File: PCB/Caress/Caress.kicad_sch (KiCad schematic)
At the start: 23 parts, among them J1 Conn_01x04_Male_Cell, J10 Conn_01x01_Male, J11 Conn_01x01_Male, J12 Conn_01x01_Male, J13 Conn_01x01_Male, J2 Conn_01x01_Male, J3 Conn_01x01_Male, J4 Conn_01x03_Male_AX12A, J5 Conn_01x02_Male_12V, J6 Conn_01x01_Male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

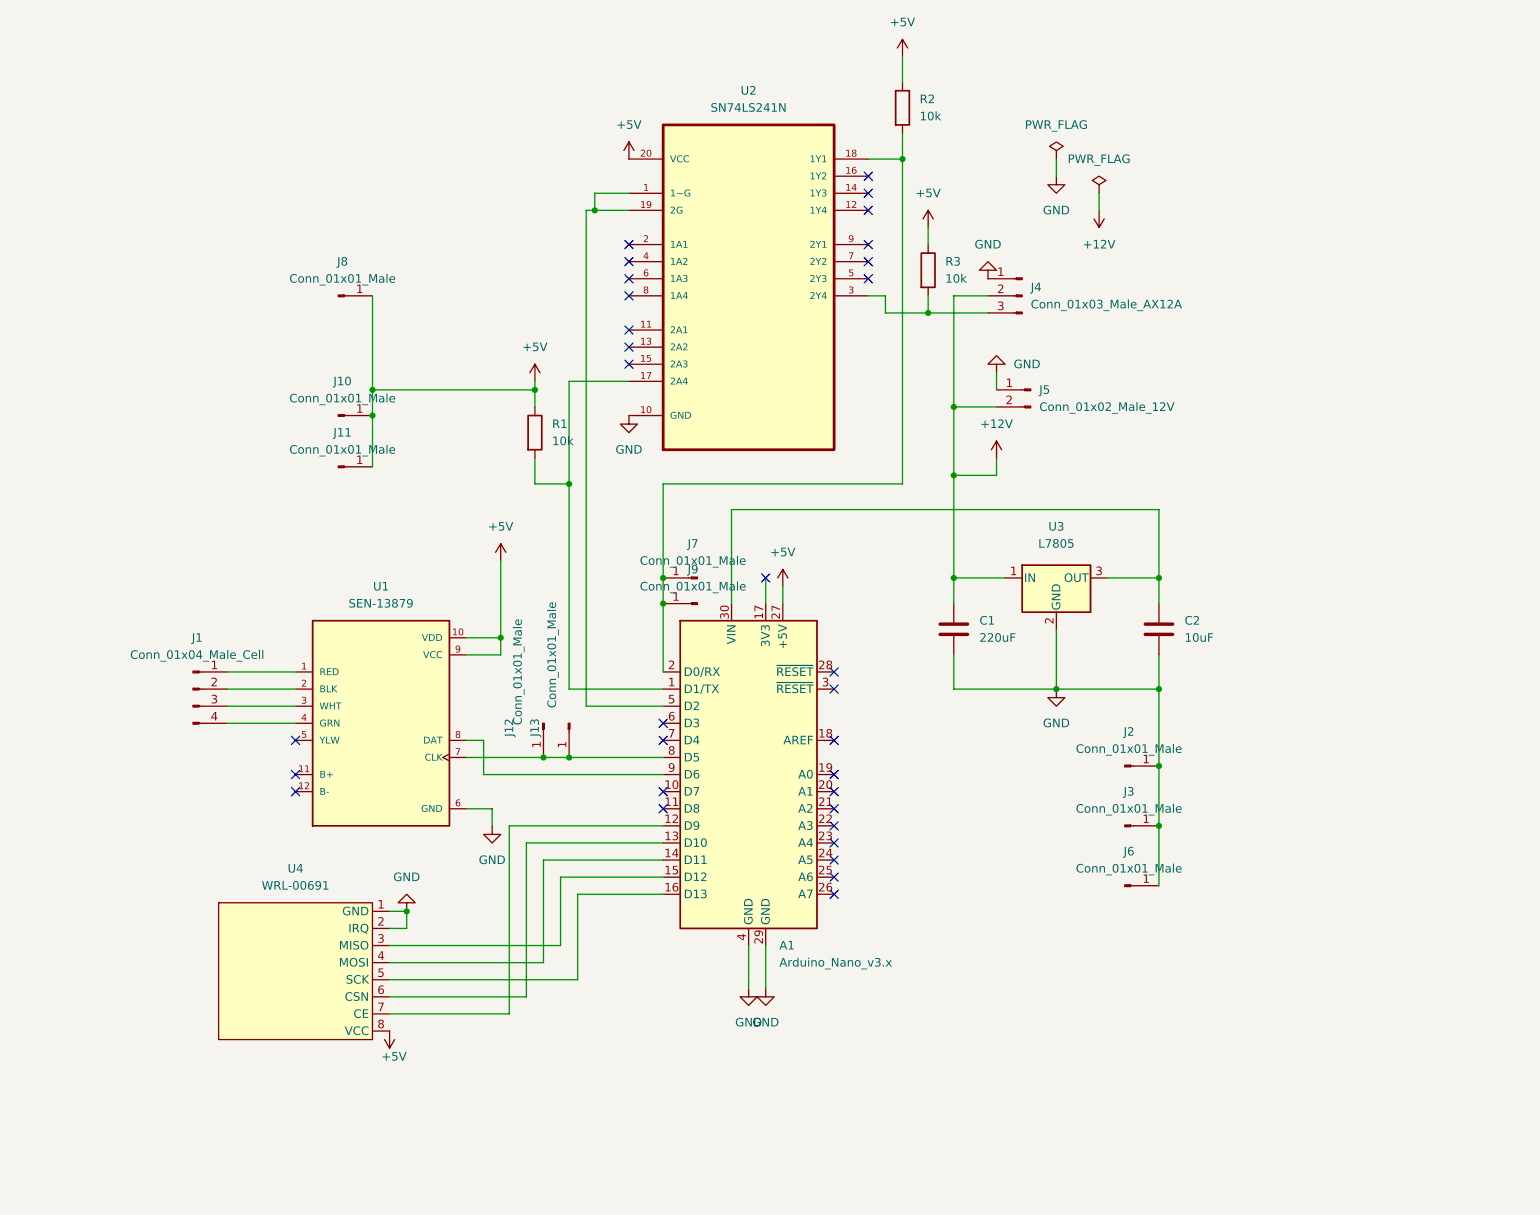
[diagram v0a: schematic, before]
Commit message: Updated PCB files; added desing files for caress and vibration
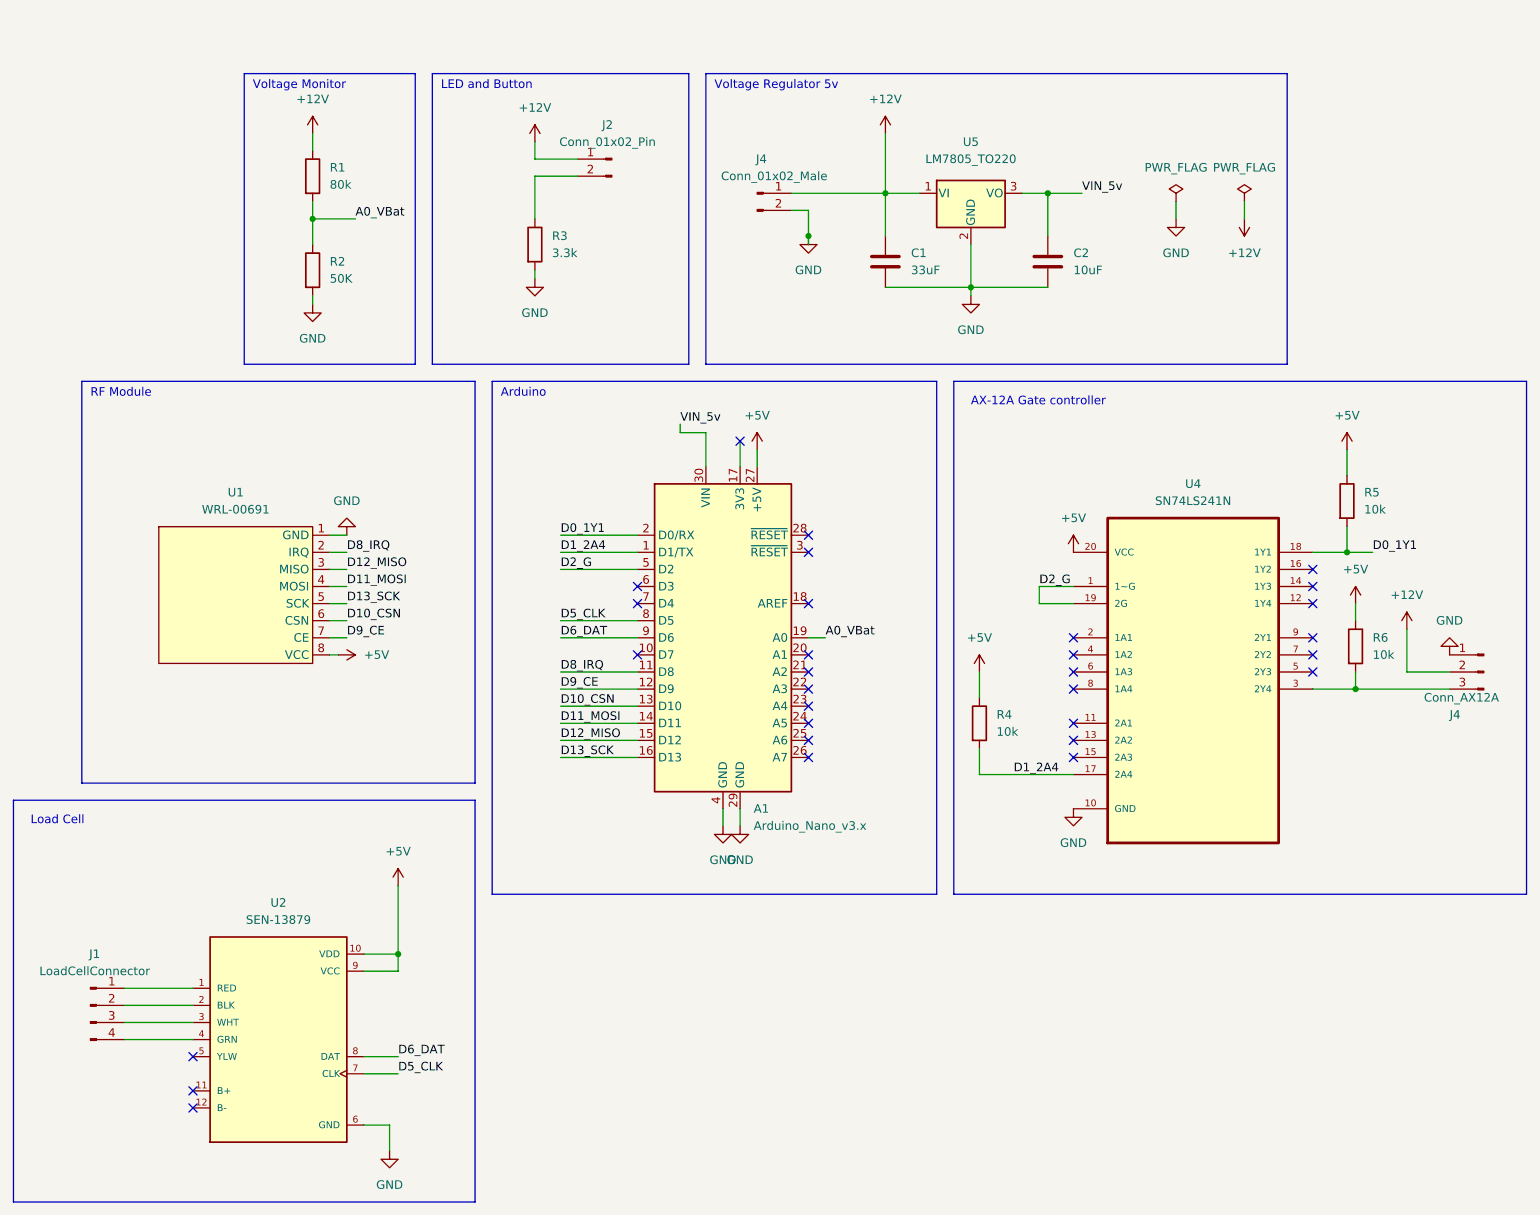
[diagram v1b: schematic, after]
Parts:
- removed J10, J11, J12, J13, J2, J3, J6, J7, J8, J9: Conn_01x01_Male, Connector_PinHeader_2.00mm:PinHeader_1x01_P2.00mm_Vertical, symbol Connector:Conn_01x01_Male
- removed J5: Conn_01x02_Male_12V, Connector_PinSocket_2.54mm:PinSocket_1x02_P2.54mm_Vertical, symbol Connector:Conn_01x02_Male
- removed U1: SEN-13879, SEN-13879:SPARKFUN_SEN-13879, symbol SEN-13879:SEN-13879
- removed U2: SN74LS241N, Package_DIP:DIP-20_W7.62mm_Socket, symbol SN74LS241N:SN74LS241N
- removed U3: L7805, Package_TO_SOT_THT:TO-220-3_Vertical, symbol Regulator_Linear:L7805
- removed U4: WRL-00691, SEN-13879:WRL-00691, symbol SN74LS241N:WRL-00691
- added J2: Conn_01x02_Pin, Connector_JST:JST_EH_B2B-EH-A_1x02_P2.50mm_Vertical, symbol Connector:Conn_01x02_Pin
- added J4: Conn_01x02_Male, Connector_JST:JST_EH_B2B-EH-A_1x02_P2.50mm_Vertical, symbol Connector:Conn_01x02_Male
- added R4, R5, R6: 10k, Resistor_THT:R_Axial_DIN0207_L6.3mm_D2.5mm_P7.62mm_Horizontal, symbol Device:R
- added U1: WRL-00691, Mods:WRL-00691, symbol SN74LS241N:WRL-00691
- added U2: SEN-13879, Mods:SPARKFUN_SEN-13879, symbol SEN-13879:SEN-13879
- added U4: SN74LS241N, Mods:DIP254P762X508-20, symbol SN74LS241N:SN74LS241N
- added U5: LM7805_TO220, Package_TO_SOT_THT:TO-220-3_Vertical, symbol Regulator_Linear:LM7805_TO220
- C1: value 220uF -> 33uF; footprint Capacitor_THT:C_Radial_D5.0mm_H11.0mm_P2.00mm -> Capacitor_THT:C_Disc_D5.0mm_W2.5mm_P5.00mm
- C2: footprint Capacitor_THT:C_Radial_D5.0mm_H11.0mm_P2.00mm -> Capacitor_THT:C_Disc_D5.0mm_W2.5mm_P5.00mm
- J1: value Conn_01x04_Male_Cell -> LoadCellConnector; footprint Connector_PinSocket_2.54mm:PinSocket_1x04_P2.54mm_Vertical -> Connector_JST:JST_EH_B4B-EH-A_1x04_P2.50mm_Vertical
- J4: value Conn_01x03_Male_AX12A -> Conn_AX12A; footprint Connector_PinSocket_2.54mm:PinSocket_1x03_P2.54mm_Vertical -> Connector_JST:JST_EH_B3B-EH-A_1x03_P2.50mm_Vertical
- R1: value 10k -> 80k; footprint Resistor_THT:R_Axial_DIN0207_L6.3mm_D2.5mm_P10.16mm_Horizontal -> Resistor_THT:R_Axial_DIN0207_L6.3mm_D2.5mm_P7.62mm_Horizontal
- R2: value 10k -> 50K; footprint Resistor_THT:R_Axial_DIN0207_L6.3mm_D2.5mm_P10.16mm_Horizontal -> Resistor_THT:R_Axial_DIN0207_L6.3mm_D2.5mm_P7.62mm_Horizontal
- R3: value 10k -> 3.3k; footprint Resistor_THT:R_Axial_DIN0207_L6.3mm_D2.5mm_P10.16mm_Horizontal -> Resistor_THT:R_Axial_DIN0207_L6.3mm_D2.5mm_P7.62mm_Horizontal
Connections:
- net +12V: now also R1.1, J2.1 (Pin_1), J4.1 (Pin_1), U5.1 (VI)
- net +5V: now also R4.1, R5.1, R6.1, U1.8 (VCC), U2.10 (VDD), U2.9 (VCC), U4.20 (VCC); no longer R1.1, R2.1, R3.1
- net GND: now also R2.2, R3.2, J4.2 (Pin_2), U1.1 (GND), U2.6 (GND), U4.10 (GND), U5.2 (GND)
- net A0_VBat: now reaches R1.2
- net A0_VBat: now also A1.19 (A0), R2.1; no longer A1.1 (D1/TX)
- net D8_IRQ: now reaches A1.11 (D8)
- net D8_IRQ: now also U1.2 (IRQ)
- net D9_CE: now reaches A1.12 (D9)
- net D9_CE: now also U1.7 (CE)
- net D10_CSN: now reaches A1.13 (D10)
- net D10_CSN: now also U1.6 (CSN)
- net D11_MOSI: now reaches A1.14 (D11)
- net D11_MOSI: now also U1.4 (MOSI)
- net D12_MISO: now reaches A1.15 (D12)
- net D12_MISO: now also U1.3 (MISO)
- net D13_SCK: now reaches A1.16 (D13)
- net D13_SCK: now also U1.5 (SCK)
- net D0_1Y1: now reaches A1.2 (D0/RX)
- net D0_1Y1: now also R5.2, U4.18 (1Y1); no longer R2.2
- net VIN_5v: now reaches A1.30 (VIN), C2.1
- net VIN_5v: now also U5.3 (VO)
- net D2_G: now reaches A1.5 (D2)
- net D2_G: now also U4.1 (1~G), U4.19 (2G)
- net D5_CLK: now reaches A1.8 (D5)
- net D5_CLK: now also U2.7 (CLK)
- net D6_DAT: now reaches A1.9 (D6)
- net D6_DAT: now also U2.8 (DAT)
- net at J4.3 (Pin_3): now also R6.2, U4.3 (2Y4); no longer R3.2
- net at J1.1 (Pin_1): now also U2.1 (RED)
- net at J1.2 (Pin_2): now also U2.2 (BLK)
- net at J1.3 (Pin_3): now also U2.3 (WHT)
- net at J1.4 (Pin_4): now also U2.4 (GRN)
- new net: J2.2 (Pin_2), R3.1
- new net D1_2A4: A1.1 (D1/TX), R4.2, U4.17 (2A4)
- no-connect marks 32 -> 30
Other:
- note added: "AX-12A Gate controller"
- note added: "Arduino"
- note added: "LED and Button"
- note added: "Load Cell"
- note added: "RF Module"
- note added: "Voltage Monitor"
- note added: "Voltage Regulator 5v"
